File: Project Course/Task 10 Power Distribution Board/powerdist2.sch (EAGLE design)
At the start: 33 parts

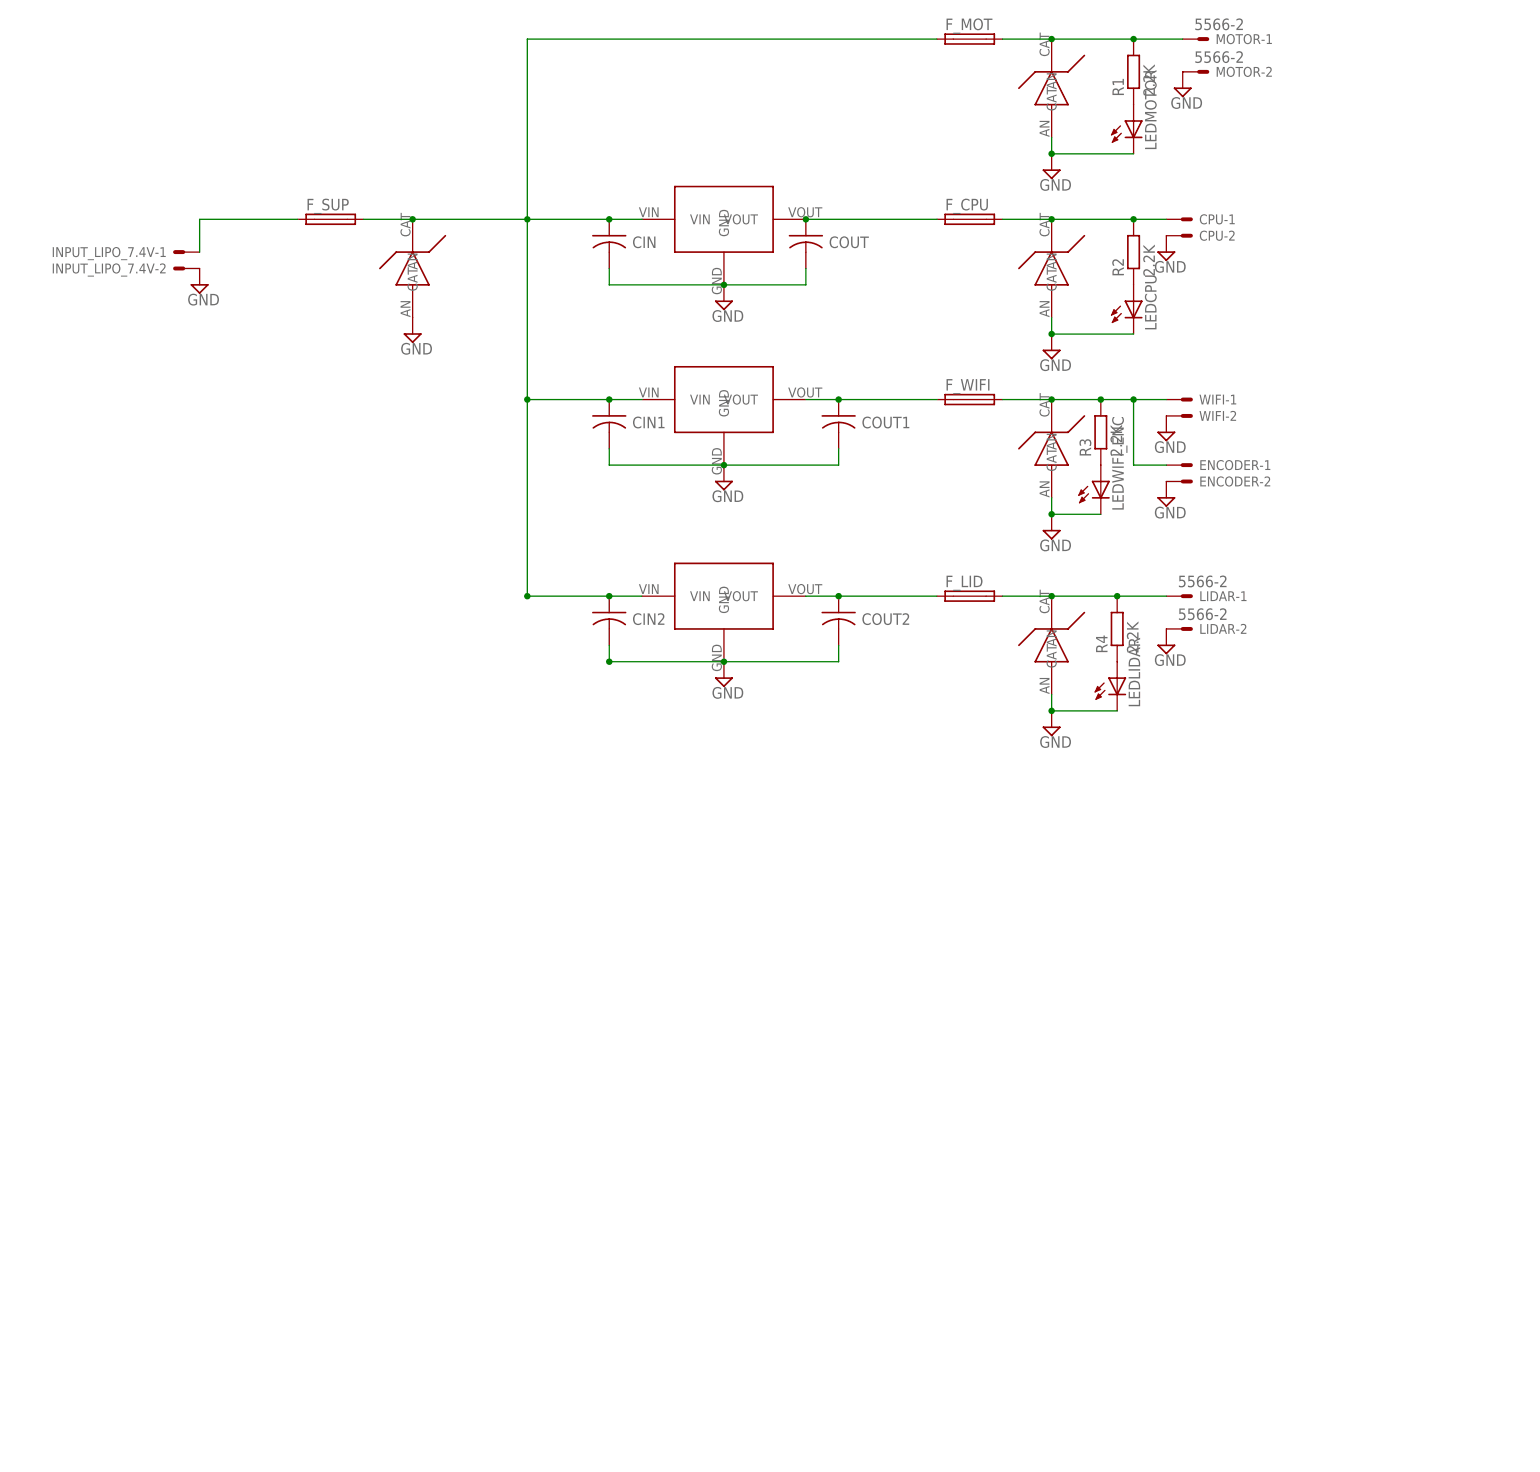
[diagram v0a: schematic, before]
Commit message: For voltage monitoring, I used a single header pin
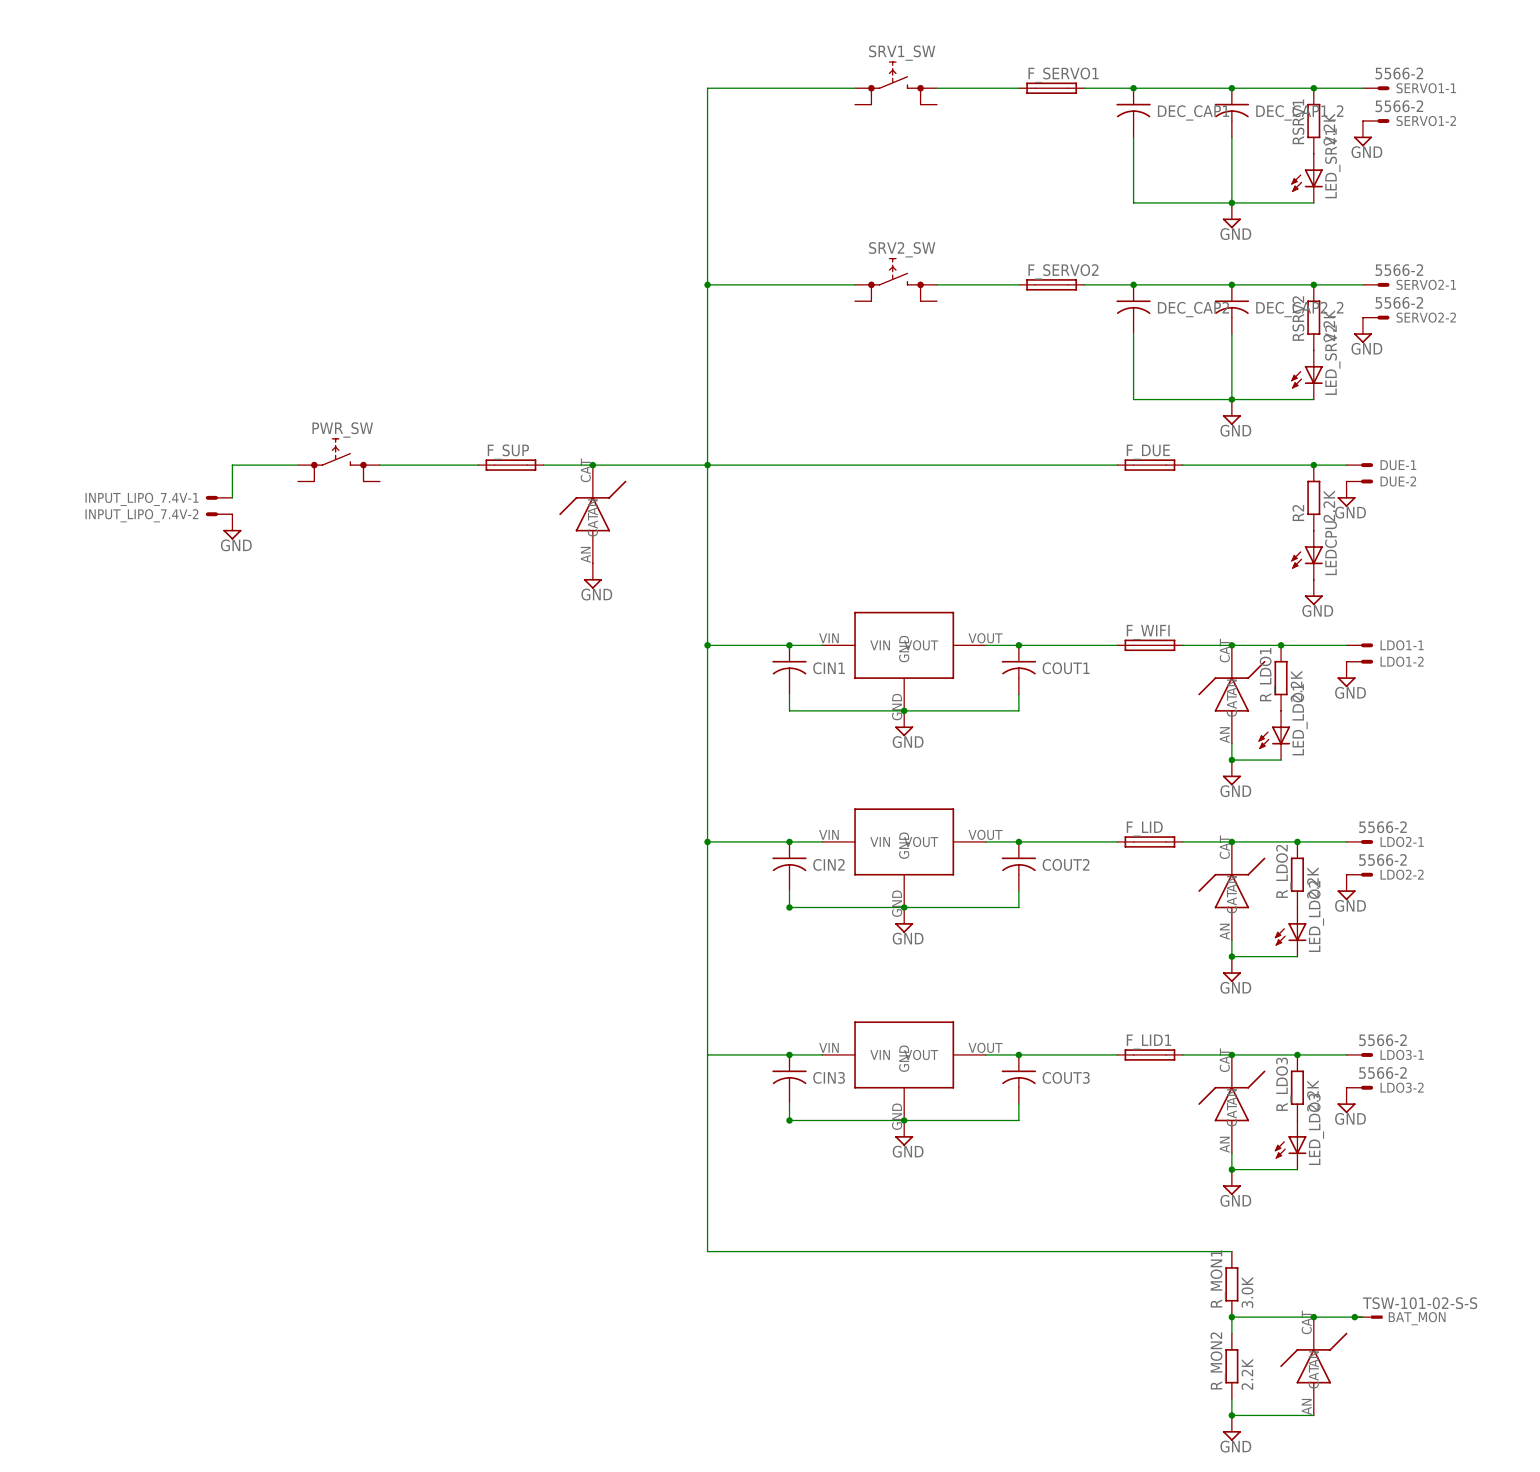
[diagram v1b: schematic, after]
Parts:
- removed CIN, COUT: CAPACITORTH_CAP, TinyGadget(1):CAPACITORTH_CAP
- removed CPU, ENCODER, WIFI: C-GRID-02-70553, con-molex:C-GRID-02-70553
- removed CPU3.3V1A: MIC29150/29300/29500, Micrel-Voltage-Regulator:MIC29150/29300/29500
- removed F_CPU, F_MOT: (no value), fuse:GSH15
- removed LEDLIDAR, LEDMOTOR, LEDWIFI_ENC: (no value), led:LEDCHIP-LED0805
- removed LIDAR, MOTOR: 5566-2, con-molex:5566-2
- removed R1, R3, R4: 2.2K, resistor:R-EU_R0402
- removed TVS-MAIN4: 26V, Micrel-Voltage-Regulator:TVS-DIODE-SMAJ
- added BAT_MON: TSW-101-02-S-S, con-samtec:TSW-101-02-S-S
- added CIN3, COUT3, DEC_CAP1, DEC_CAP1_2, DEC_CAP2, DEC_CAP2_2: CAPACITORTH_CAP, TinyGadget(1):CAPACITORTH_CAP
- added DUE, LDO1: C-GRID-02-70553, con-molex:C-GRID-02-70553
- added F_DUE, F_LID1, F_SERVO1, F_SERVO2: (no value), fuse:GSH15
- added LDO2, LDO3, SERVO1, SERVO2: 5566-2, con-molex:5566-2
- added LED_LDO1, LED_LDO2, LED_LDO3, LED_SRV1, LED_SRV2: (no value), led:LEDCHIP-LED0805
- added LID12V1A1: MIC29150/29300/29500, Micrel-Voltage-Regulator:MIC29150/29300/29500
- added PWR_SW, SRV1_SW, SRV2_SW: (no value), switch:REKN
- added RSRV1, RSRV2, R_LDO1, R_LDO2, R_LDO3, R_MON2: 2.2K, resistor:R-EU_R0402
- added R_MON1: 3.0K, resistor:R-EU_R0402
- added TVS_3.3: 16V, Micrel-Voltage-Regulator:TVS-DIODE-SMAJ
- TVS-MAIN1: value 3.3V -> 16V
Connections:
- new net N$14: F_SUP.1, PWR_SW.1@A
- new net N$15: DEC_CAP1.1, DEC_CAP1_2.1, F_SERVO1.2, RSRV1.2, SERVO1-1.S
- new net N$16: LED_SRV1.A, RSRV1.1
- new net N$17: F_SERVO2.1, SRV2_SW.1@A
- new net N$18: BAT_MON.1, R_MON1.1, R_MON2.2, TVS_3.3.CAT
- new net N$19: COUT3.1, F_LID1.1, LID12V1A1.VOUT
- new net N$20: CIN3.1, LID12V1A1.VIN
- new net N$21: F_LID1.2, LDO3-1.S, R_LDO3.2, TVS-MAIN1.CAT
- new net N$22: LED_LDO3.A, R_LDO3.1
- net GND: now also CIN3.2, COUT3.2, DEC_CAP1.2, DEC_CAP1_2.2, DEC_CAP2.2, DEC_CAP2_2.2, DUE-2.S, LDO1-2.S, LDO2-2.S, LDO3-2.S, LED_LDO1.C, LED_LDO2.C, LED_LDO3.C, LED_SRV1.C, LED_SRV2.C, LID12V1A1.GND, R_MON2.1, SERVO1-2.S, SERVO2-2.S, TVS_3.3.AN; no longer CIN.2, COUT.2, CPU-2.S, CPU3.3V1A.GND, ENCODER-2.S, LEDLIDAR.C, LEDMOTOR.C, LEDWIFI_ENC.C, LIDAR-2.S, MOTOR-2.S, TVS-MAIN4.AN, WIFI-2.S
- net N$1: now also DEC_CAP2.1, DEC_CAP2_2.1, F_SERVO2.2, RSRV2.2, SERVO2-1.S; no longer F_MOT.2, MOTOR-1.S, R1.2, TVS-MAIN4.CAT
- net N$10: now also PWR_SW.0@A; no longer F_SUP.1
- net N$11: now also LED_LDO1.A, R_LDO1.1; no longer LEDWIFI_ENC.A, R3.1
- net N$12: now also F_DUE.1, R_MON1.2, SRV1_SW.0@A, SRV2_SW.0@A; no longer CIN.1, CPU3.3V1A.VIN, F_MOT.1
- net N$13: now also LED_LDO2.A, R_LDO2.1; no longer LEDLIDAR.A, R4.1
- net N$2: now also LDO2-1.S, R_LDO2.2; no longer LIDAR-1.S, R4.2
- net N$3: now also F_SERVO1.1, SRV1_SW.1@A; no longer COUT.1, CPU3.3V1A.VOUT, F_CPU.1
- net N$4: now also DUE-1.S, F_DUE.2; no longer CPU-1.S, F_CPU.2, TVS-MAIN1.CAT
- net N$5: now also LED_SRV2.A, RSRV2.1; no longer LEDMOTOR.A, R1.1
- net N$7: now also LDO1-1.S, R_LDO1.2; no longer ENCODER-1.S, R3.2, WIFI-1.S
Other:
- moved on the sheet: CIN1, CIN2, COUT1, COUT2, F_LID, F_SUP, F_WIFI, INPUT_LIPO_7.4V-1, INPUT_LIPO_7.4V-2, LEDCPU, R2
